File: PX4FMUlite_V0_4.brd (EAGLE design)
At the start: 48.6 x 34.9 mm, 126 parts, among them J2 DF13-4P-1.25V, J201 DF13C-6P-1.25V, J202 DF13C-6P-1.25V, J203 DF13C-6P-1.25V, J3 DF13C-4P-1.25V, J302 DF13C-4P-1.25V, J401 DF13C-4P-1.25V, J403 DF13C-7P-1.25V, J405 DF13C-4P-1.25V, J802 DF13C-3P-1.25V, M3_MOUNT1101 MOUNT-HOLE3.1MM, M3_MOUNT1102 MOUNT-HOLE3.1MM, M3_MOUNT1103 MOUNT-HOLE3.1MM, M3_MOUNT1104 MOUNT-HOLE3.1MM, U101 STM32F4X7VX, U2 MAX3051, U401 MAX3051, X101 3.2x2.5 mm / 24 MHz / 15 ppm

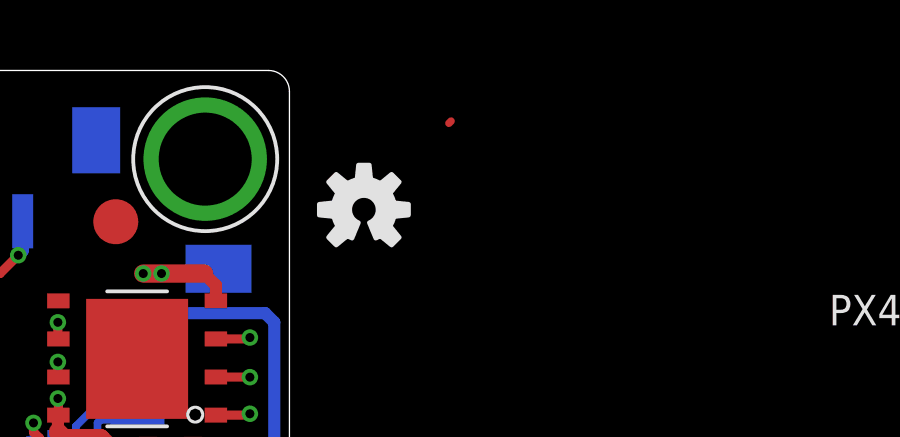
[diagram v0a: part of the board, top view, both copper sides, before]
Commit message: Removed random track spot outside of dimensions
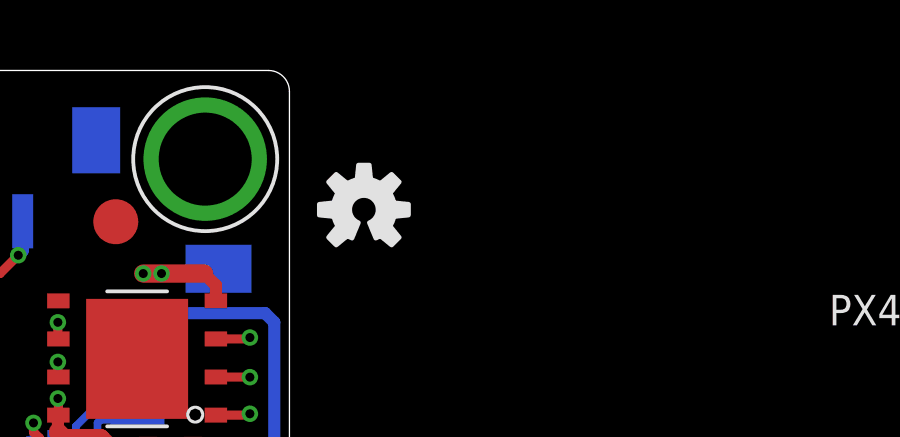
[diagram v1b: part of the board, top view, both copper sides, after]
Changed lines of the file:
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@@
 <contactref element="U$5" pad="5"/>
 <contactref element="U101" pad="68"/>
-<wire x1="63.1952" y1="35.9664" x2="63.1244" y2="35.8956" width="0.254" layer="1"/>
 <contactref element="D1" pad="ANODE"/>
 <wire x1="47.0408" y1="35.219" x2="47.0408" y2="36.068" width="0.254" layer="1"/>
@@
 <wire x1="44.6024" y1="33.9344" x2="44.2976" y2="33.6296" width="0.6096" layer="1"/>
 <wire x1="44.2976" y1="33.6296" x2="44.2976" y2="32.6136" width="0.6096" layer="1"/>
-<wire x1="47.0408" y1="35.219" x2="63.1244" y2="35.8956" width="0" layer="19" extent="1-1"/>
 </signal>
 <signal name="VDD_5V_PERIPH" class="1">
